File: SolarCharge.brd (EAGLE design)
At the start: 63 x 63 mm, 14 parts, among them U1 TINY4/5/9/10-TSHR/TS8R

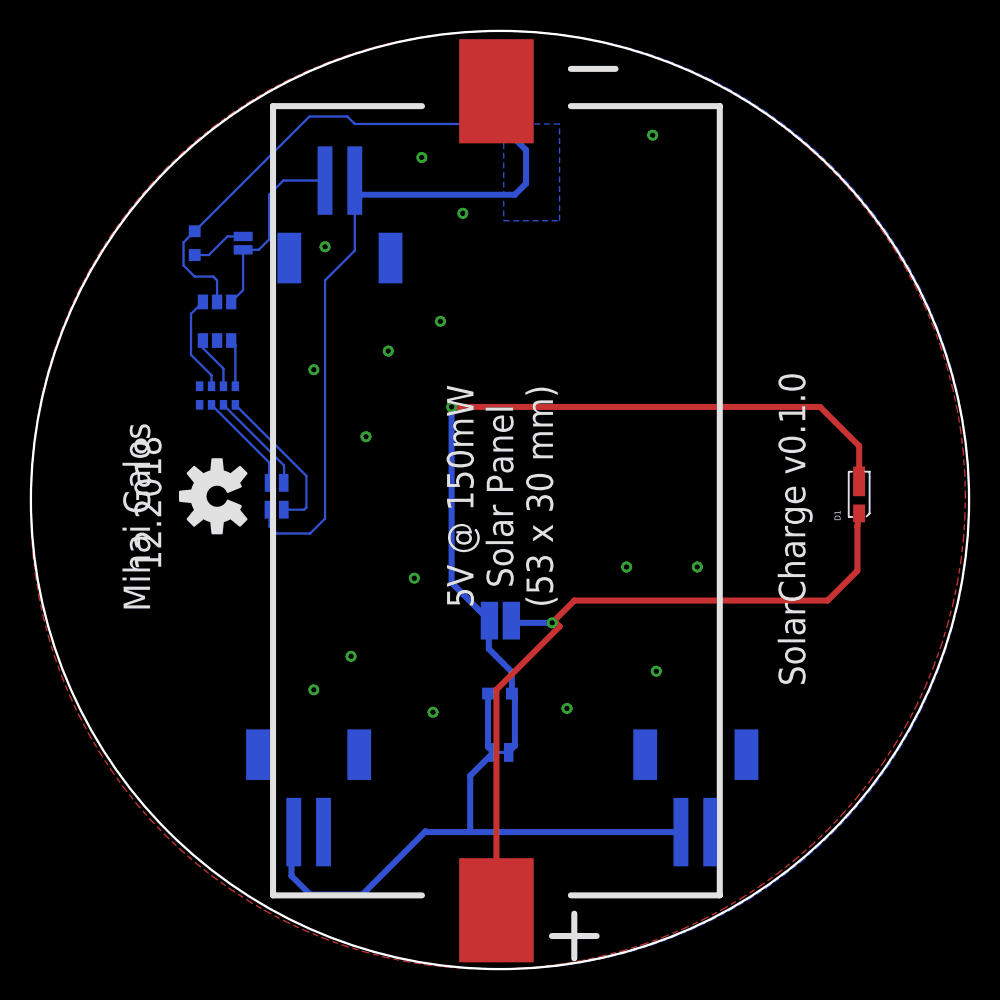
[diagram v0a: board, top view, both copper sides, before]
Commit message: Add p-channel mosfet for latching boost converter
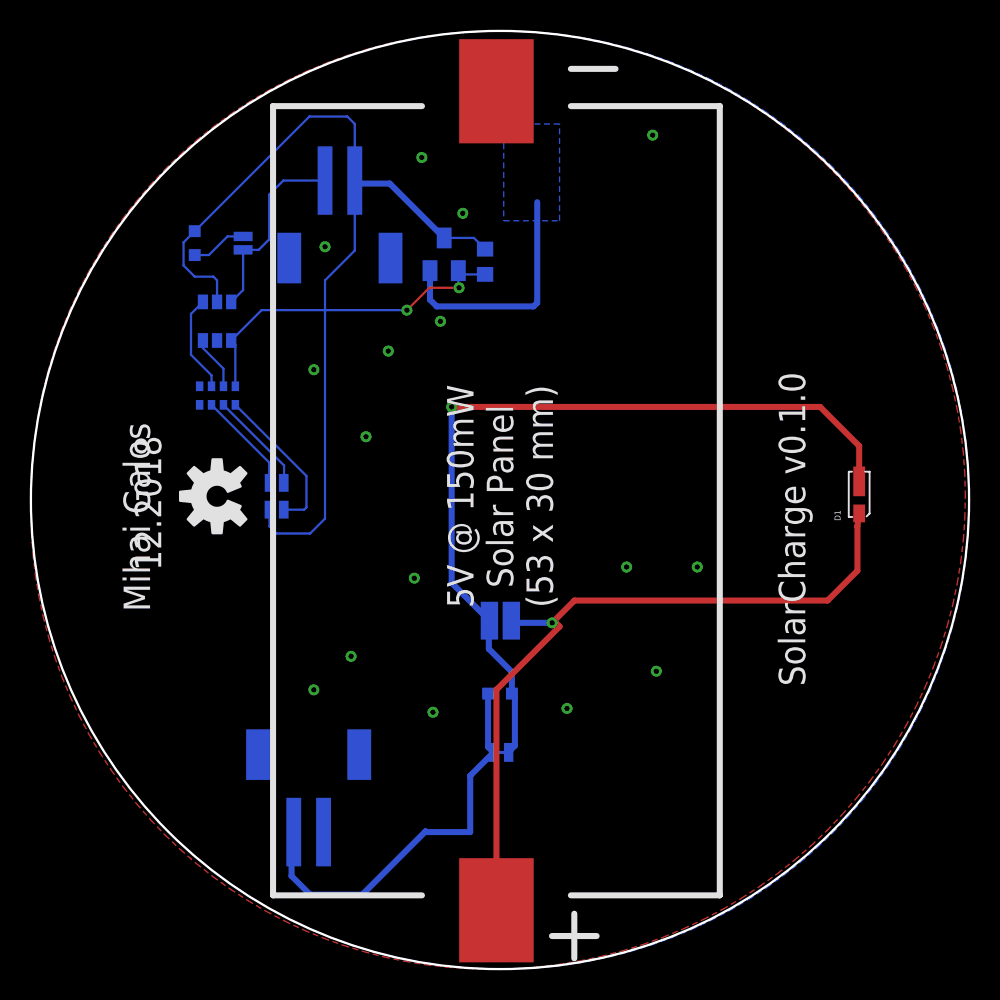
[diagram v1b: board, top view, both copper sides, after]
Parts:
- removed CN3: (no value), lio:JST-PH-2-SMT-RA
- added Q1: (no value), adafruit:SOT23
- added R6: (no value), rcl:R0603
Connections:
- new net BOOST_CONVERTER_INPUT: Q1.2
- net +3V3: now also Q1.3, R6.2
- net GND: no longer CN3.2
- net N$4: no longer CN3.1
- net RED: now also Q1.1, R6.1
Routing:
- net RED: track 3.58 -> 23.4 mm, vias 0 -> 2
- net BOOST_CONVERTER_INPUT: track 0.00 -> 16.2 mm
- net N$4: track 41.6 -> 27.4 mm
- net +3V3: track 76.1 -> 64.2 mm
- added copper zone on layer 16, net BOOST_CONVERTER_INPUT
- removed copper zone on layer 16, net +3V3
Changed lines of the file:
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@@
 <element name="CN2" library="lio" package="JST-PH-2-SMT-RA" value="" x="9.75" y="49" rot="MR180"/>
 <element name="SJ2" library="SparkFun-Passives" package="SJ_2S-NO" value="SOLDERJUMPERNO" x="3.25" y="48.5" rot="MR90"/>
-<element name="CN3" library="lio" package="JST-PH-2-SMT-RA" value="" x="33.65" y="12.65" rot="MR0"/>
+<element name="R6" library="rcl" package="R0603" value="" x="19.5" y="47.25" rot="MR90"/>
+<element name="Q1" library="adafruit" package="SOT23" value="" x="16.75" y="47.75" rot="MR0"/>
 </elements>
 <signals>
@@
 <via x="8" y="40" extent="1-16" drill="0.35"/>
 <contactref element="U1" pad="2"/>
-<contactref element="CN3" pad="2"/>
 <via x="11.5" y="35.5" extent="1-16" drill="0.35"/>
 <via x="16.5" y="43.25" extent="1-16" drill="0.35"/>
@@
 <via x="14.75" y="26" extent="1-16" drill="0.35"/>
 <via x="8" y="18.5" extent="1-16" drill="0.35"/>
+<wire x1="22.5" y1="56.46" x2="30.75" y2="55.75" width="0" layer="19" extent="1-1"/>
+<wire x1="15.25" y1="54.25" x2="20.26" y2="58.7" width="0" layer="19" extent="1-1"/>
+<wire x1="18" y1="50.5" x2="15.25" y2="54.25" width="0" layer="19" extent="1-1"/>
+<wire x1="16.5" y1="43.25" x2="18" y2="50.5" width="0" layer="19" extent="1-1"/>
+<wire x1="13" y1="41.25" x2="16.5" y2="43.25" width="0" layer="19" extent="1-1"/>
+<wire x1="8" y1="40" x2="13" y2="41.25" width="0" layer="19" extent="1-1"/>
+<wire x1="11.5" y1="35.5" x2="8" y2="40" width="0" layer="19" extent="1-1"/>
+<wire x1="1.5" y1="41.96" x2="8" y2="40" width="0" layer="19" extent="16-16"/>
+<wire x1="8.75" y1="48.25" x2="13" y2="41.25" width="0" layer="19" extent="1-1"/>
+<wire x1="14.75" y1="26" x2="11.5" y2="35.5" width="0" layer="19" extent="1-1"/>
+<wire x1="10.5" y1="20.75" x2="14.75" y2="26" width="0" layer="19" extent="1-1"/>
+<wire x1="8" y1="18.5" x2="10.5" y2="20.75" width="0" layer="19" extent="1-1"/>
+<wire x1="16" y1="17" x2="10.5" y2="20.75" width="0" layer="19" extent="1-1"/>
+<wire x1="25" y1="17.25" x2="16" y2="17" width="0" layer="19" extent="1-1"/>
+<wire x1="31" y1="19.75" x2="25" y2="17.25" width="0" layer="19" extent="1-1"/>
+<wire x1="29" y1="26.75" x2="31" y2="19.75" width="0" layer="19" extent="1-1"/>
+<wire x1="33.75" y1="26.75" x2="29" y2="26.75" width="0" layer="19" extent="1-1"/>
+<wire x1="8.65" y1="8.95" x2="8" y2="18.5" width="0" layer="19" extent="16-16"/>
 </signal>
 <signal name="N$3">
@@
 <contactref element="R1" pad="2"/>
 <contactref element="CN1" pad="1"/>
-<contactref element="CN3" pad="1"/>
 <wire x1="20.067" y1="14.3" x2="19.7" y2="14.667" width="0.4064" layer="16"/>
 <wire x1="19.7" y1="14.667" x2="19.7" y2="18.25" width="0.4064" layer="16"/>
-<wire x1="32.65" y1="8.95" x2="18.5" y2="8.95" width="0.4064" layer="16"/>
 <wire x1="18.5" y1="8.95" x2="15.55" y2="8.95" width="0.4064" layer="16"/>
 <wire x1="15.55" y1="8.95" x2="15.5" y2="9" width="0.4064" layer="16"/>
@@
 <wire x1="8.75" y1="46" x2="10.75" y2="48" width="0.1524" layer="16"/>
 <wire x1="10.75" y1="48" x2="10.75" y2="51.75" width="0.1524" layer="16"/>
-<wire x1="10.75" y1="51.75" x2="10.75" y2="52.7" width="0.1524" layer="16"/>
+<wire x1="10.75" y1="51.75" x2="10.75" y2="52.5" width="0.1524" layer="16"/>
+<wire x1="10.75" y1="52.5" x2="10.75" y2="52.7" width="0.1524" layer="16"/>
 <wire x1="8.75" y1="30" x2="8.75" y2="46" width="0.1524" layer="16"/>
 <wire x1="5.0225" y1="30.6" x2="5.0225" y2="29.4775" width="0.1524" layer="16"/>
@@
 <wire x1="-0.75" y1="47" x2="0" y2="46.25" width="0.1524" layer="16"/>
 <wire x1="1.5" y1="46" x2="1.5" y2="44.55" width="0.1524" layer="16"/>
-<polygon width="0.2" layer="16">
-<vertex x="20.75" y="50"/>
-<vertex x="24.5" y="50"/>
-<vertex x="24.5" y="56.5"/>
-<vertex x="20.75" y="56.5"/>
-</polygon>
-<wire x1="10.75" y1="56.5" x2="20.5" y2="56.5" width="0.1524" layer="16"/>
-<wire x1="20.5" y1="56.5" x2="22.25" y2="54.75" width="0.4064" layer="16"/>
-<wire x1="22.25" y1="54.75" x2="22.25" y2="52.5" width="0.4064" layer="16"/>
-<wire x1="22.25" y1="52.5" x2="21.5" y2="51.75" width="0.4064" layer="16"/>
-<wire x1="21.5" y1="51.75" x2="10.75" y2="51.75" width="0.4064" layer="16"/>
+<contactref element="R6" pad="2"/>
+<contactref element="Q1" pad="3"/>
+<wire x1="10.75" y1="56.5" x2="10.75" y2="52.7" width="0.1524" layer="16"/>
+<wire x1="19.5" y1="48.1" x2="18.75" y2="48.85" width="0.1524" layer="16"/>
+<wire x1="18.75" y1="48.85" x2="16.75" y2="48.85" width="0.1524" layer="16"/>
+<wire x1="16.75" y1="48.85" x2="13.1" y2="52.5" width="0.4064" layer="16"/>
+<wire x1="13.1" y1="52.5" x2="10.75" y2="52.5" width="0.4064" layer="16"/>
 </signal>
 <signal name="RED_RESISTOR">
@@
 <wire x1="2.72875" y1="38.88875" x2="2.72875" y2="41.68125" width="0.1524" layer="16"/>
 <wire x1="2.72875" y1="41.68125" x2="2.45" y2="41.96" width="0.1524" layer="16"/>
+<contactref element="R6" pad="1"/>
+<contactref element="Q1" pad="1"/>
+<wire x1="17.7" y1="46.65" x2="17.7" y2="45.55" width="0.1524" layer="16"/>
+<wire x1="17.7" y1="45.55" x2="17.75" y2="45.5" width="0.1524" layer="16"/>
+<via x="17.75" y="45.5" extent="1-16" drill="0.35"/>
+<wire x1="17.75" y1="45.5" x2="15.75" y2="45.5" width="0.1524" layer="1"/>
+<wire x1="15.75" y1="45.5" x2="14.25" y2="44" width="0.1524" layer="1"/>
+<via x="14.25" y="44" extent="1-16" drill="0.35"/>
+<wire x1="14.25" y1="44" x2="4.49" y2="44" width="0.1524" layer="16"/>
+<wire x1="4.49" y1="44" x2="2.45" y2="41.96" width="0.1524" layer="16"/>
+<wire x1="19.5" y1="46.4" x2="17.95" y2="46.4" width="0.1524" layer="16"/>
+<wire x1="17.95" y1="46.4" x2="17.7" y2="46.65" width="0.1524" layer="16"/>
 </signal>
 <signal name="BLUE">
@@
 <wire x1="2.2" y1="48.95" x2="0.95" y2="47.7" width="0.1524" layer="16"/>
 </signal>
+<signal name="BOOST_CONVERTER_INPUT">
+<contactref element="Q1" pad="2"/>
+<wire x1="15.8" y1="46.65" x2="15.8" y2="44.7" width="0.4064" layer="16"/>
+<wire x1="15.8" y1="44.7" x2="16.25" y2="44.25" width="0.4064" layer="16"/>
+<wire x1="16.25" y1="44.25" x2="22.75" y2="44.25" width="0.4064" layer="16"/>
+<wire x1="22.75" y1="44.25" x2="23" y2="44.5" width="0.4064" layer="16"/>
+<wire x1="23" y1="44.5" x2="23" y2="51.25" width="0.4064" layer="16"/>
+<polygon width="0.2" layer="16">
+<vertex x="20.75" y="50"/>
+<vertex x="24.5" y="50"/>
+<vertex x="24.5" y="56.5"/>
+<vertex x="20.75" y="56.5"/>
+</polygon>
+</signal>
 </signals>

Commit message: Add overvoltage protection
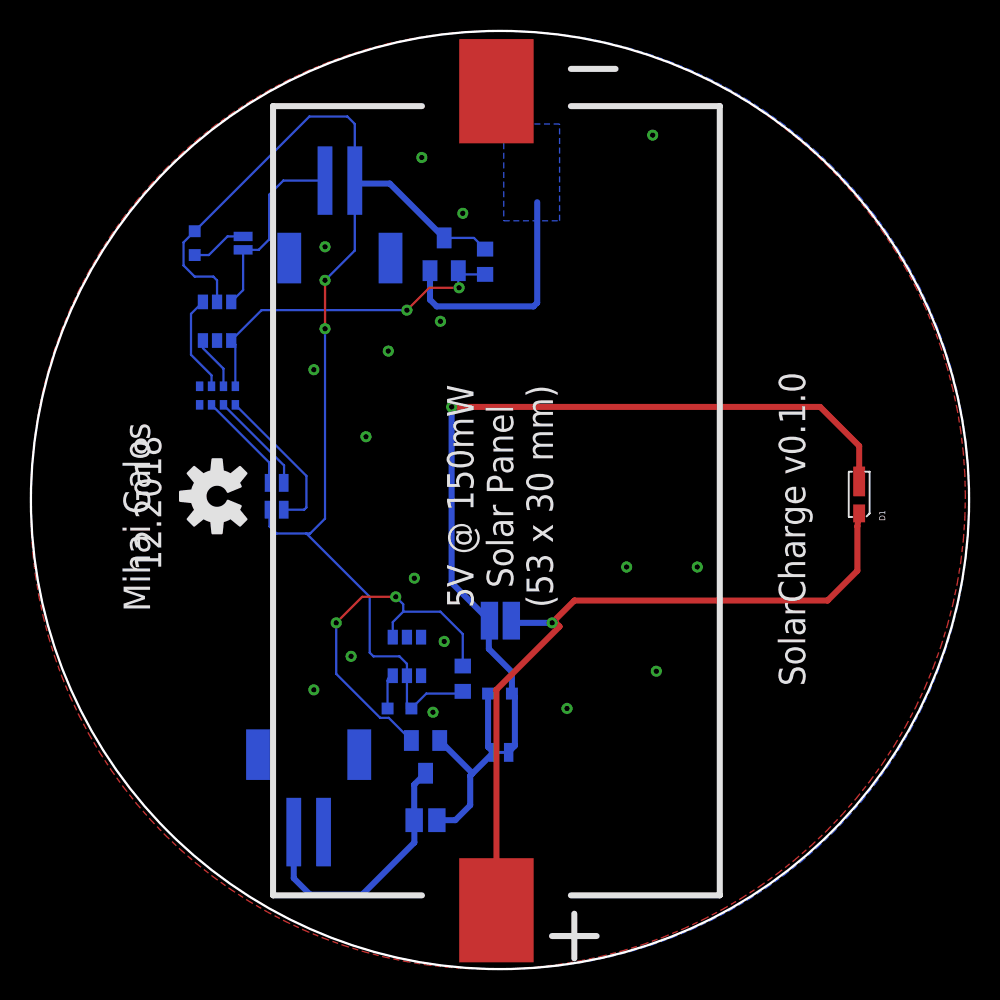
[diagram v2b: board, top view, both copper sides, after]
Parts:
- added Q2: (no value), adafruit:SOT23
- added R4: (no value), rcl:R0603
- added R5: (no value), ROHM:0603-RES
- added SJ4: (no value), jumper:SJ
- added U2: TINY4/5/9/10-TSHR/TS8R, bt_avr:SOT-23-6
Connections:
- new net N$10: Q2.1, R4.1, U2.1
- new net N$11: R5.2, U2.6
- new net N$9: CN1.1, Q2.3, SJ4.2
- net +3V3: now also R4.2, R5.1, U2.5
- net GND: now also U2.2
- net N$4: now also Q2.2, SJ4.1; no longer CN1.1
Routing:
- net N$10: track 0.00 -> 25.0 mm, vias 0 -> 2
- net +3V3: track 64.2 -> 84.0 mm, vias 0 -> 2
- net N$9: track 0.00 -> 18.1 mm
- net N$4: track 27.4 -> 14.1 mm
- net N$11: track 0.00 -> 2.34 mm
- net GND: vias 16 -> 17
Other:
- board text removed: "Fallback to 0603 led."
